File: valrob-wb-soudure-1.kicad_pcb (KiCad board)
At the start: 2 copper layers, 85 x 50 mm, 35 parts, among them J1 Conn_01x03, J2 Conn_01x06, J3 Conn_01x02, J4 Conn_01x02, J5 Conn_01x02, J6 Conn_01x02, Q1 2N7000, SW1 SW_Push, SW2 SW_Push, SW3 SW_Push, SW4 SW_Push

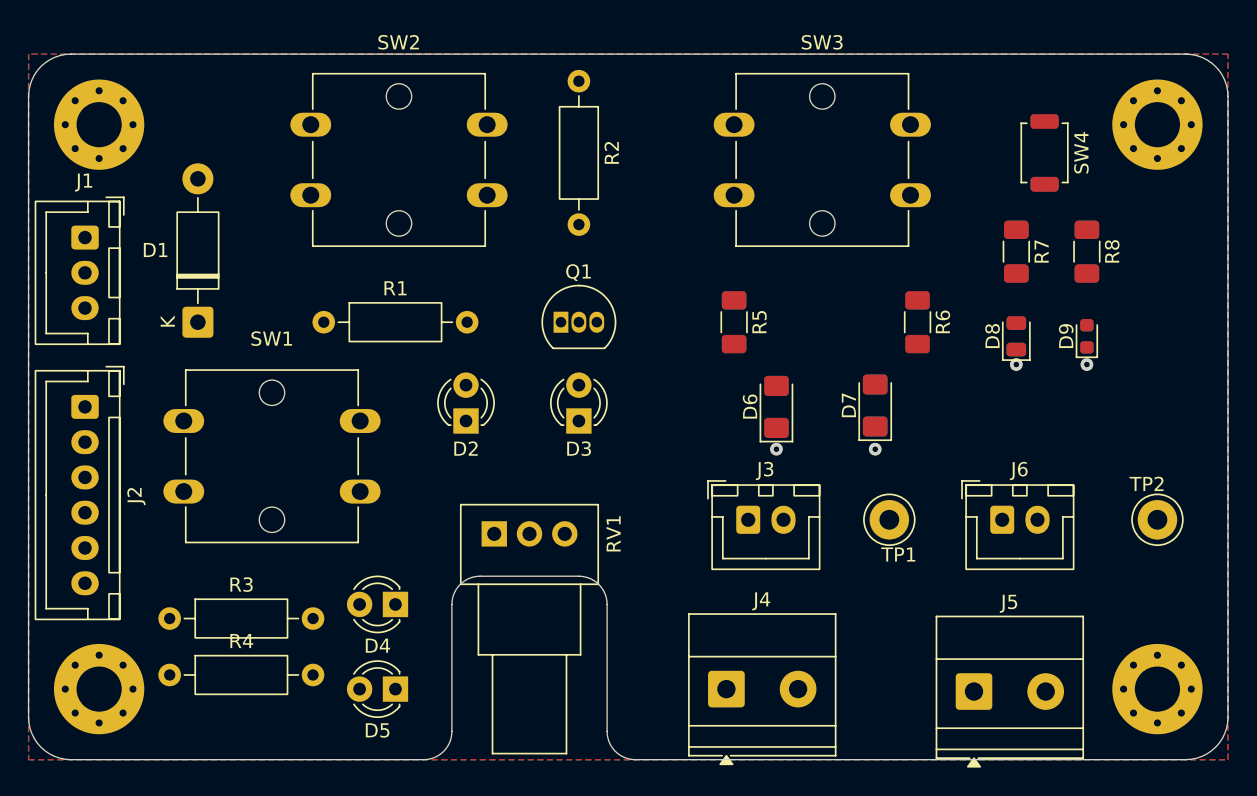
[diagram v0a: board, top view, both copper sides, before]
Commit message: pcb: add routing
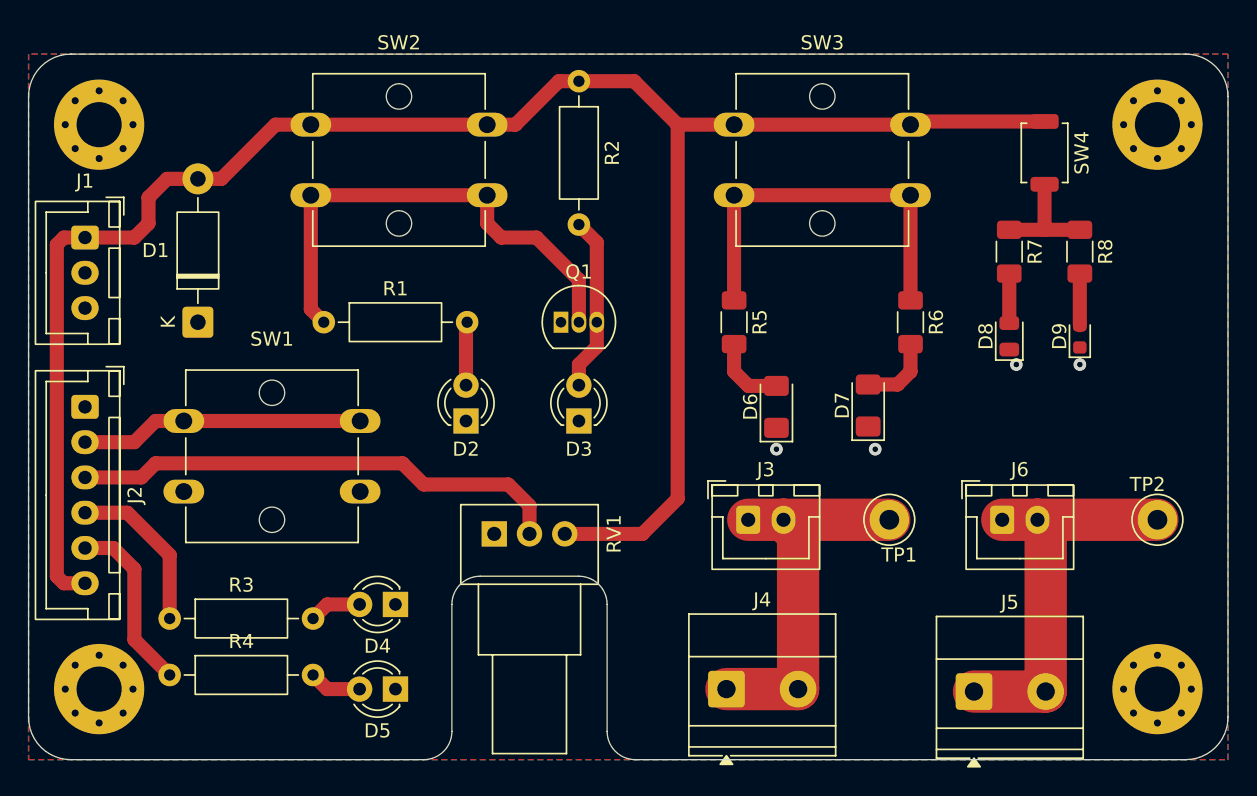
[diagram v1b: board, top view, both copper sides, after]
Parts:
- moved D7 0.50 mm to (107.5, 117.9)
- moved D8 0.50 mm to (117.5, 113.0)
- moved D9 0.50 mm to (122.5, 113.0)
- moved R6 0.50 mm to (110.5, 112.0)
- moved R7 0.50 mm to (117.5, 107.0)
- moved R8 0.50 mm to (122.5, 107.0)
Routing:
- net +5V: track 0.00 -> 138.5 mm
- net Net-(J2-Pin_3): track 0.00 -> 35.2 mm
- net Net-(Q1-G): track 0.00 -> 35.0 mm
- net Net-(J5-Pin_1): track 0.00 -> 28.5 mm
- net Net-(J3-Pin_1): track 0.00 -> 27.5 mm
- net Net-(R5-Pad1): track 0.00 -> 27.4 mm
- net Net-(J2-Pin_2): track 0.00 -> 20.1 mm
- net /RED: track 0.00 -> 12.7 mm
- net Net-(D3-A): track 0.00 -> 12.4 mm
- net /BLUE: track 0.00 -> 11.7 mm
- net Net-(R7-Pad1): track 0.00 -> 8.23 mm
- net Net-(D6-A): track 0.00 -> 5.37 mm
- net Net-(D7-A): track 0.00 -> 5.33 mm
- net Net-(D2-A): track 0.00 -> 4.49 mm
- net Net-(D5-A): track 0.00 -> 3.71 mm
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
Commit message: pcb(silk): clean reference designators
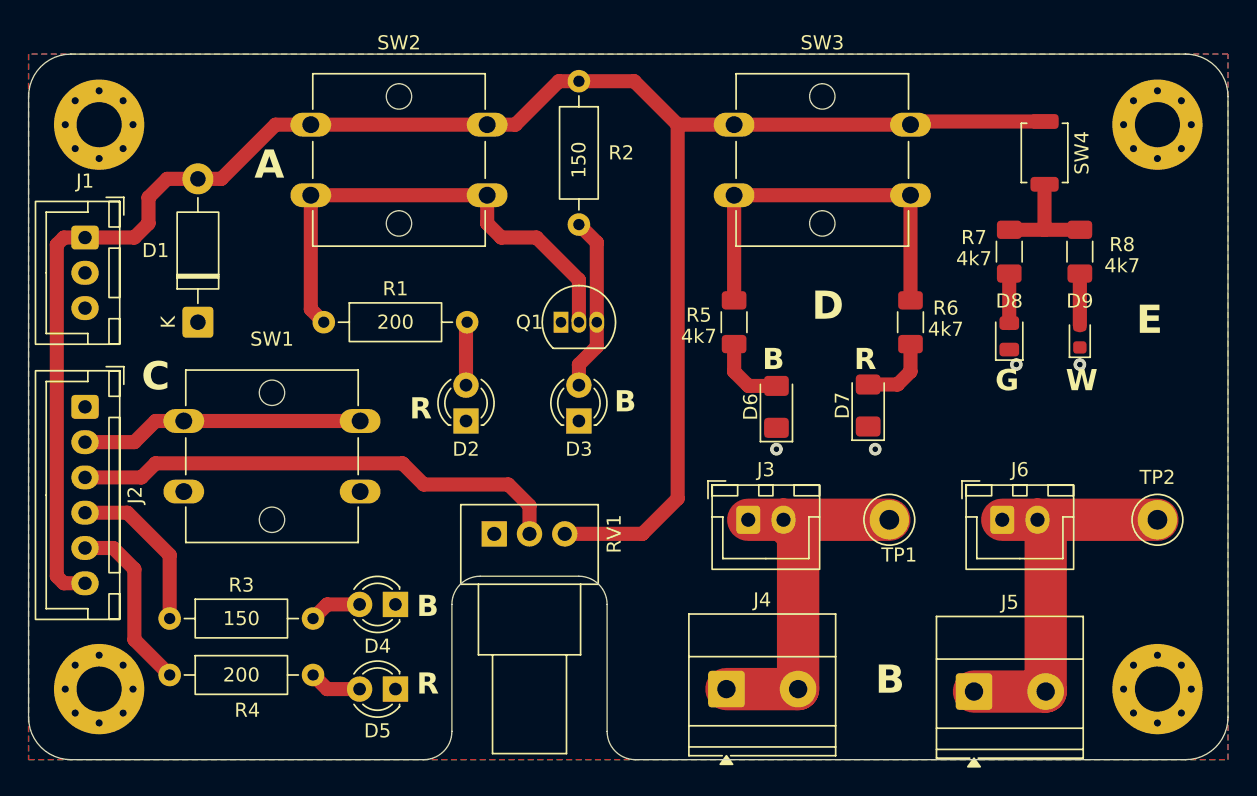
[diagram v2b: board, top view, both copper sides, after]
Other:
- board text added: "A"
- board text added: "B"
- board text added: "C"
- board text added: "D"
- board text added: "E"
- board text added: "G"
- board text added: "R"
- board text added: "W"
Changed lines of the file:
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@@
 		(tags "resistor handsolder")
 		(property "Reference" "R7"
-			(at 0 -1.83 90)
+			(at -1 2.5 180)
 			(layer "F.SilkS")
 			(effects
@@
 		)
 		(property "Value" "4k7"
-			(at 0 1.83 90)
-			(layer "F.Fab")
+			(at 0.5 2.5 180)
+			(layer "F.SilkS")
 			(effects
 				(font
@@
 		(tags "resistor handsolder")
 		(property "Reference" "R6"
-			(at 0 -1.83 90)
+			(at -1 -2.5 0)
 			(layer "F.SilkS")
 			(effects
@@
 		)
 		(property "Value" "4k7"
-			(at 0 1.83 90)
-			(layer "F.Fab")
+			(at 0.5 -2.5 0)
+			(layer "F.SilkS")
 			(effects
 				(font
@@
 		(tags "LED")
 		(property "Reference" "D8"
-			(at 0 -1.65 90)
+			(at 2.5 0 180)
 			(layer "F.SilkS")
 			(effects
@@
 		)
 		(property "Value" "200"
-			(at 5.08 2.37 0)
-			(layer "F.Fab")
+			(at 5.08 0 0)
+			(layer "F.SilkS")
 			(effects
 				(font
@@
 		(tags "LED")
 		(property "Reference" "D9"
-			(at 0 -1.43 90)
+			(at 2.5 0 180)
 			(layer "F.SilkS")
 			(effects
@@
 		(tags "test point wire loop bead")
 		(property "Reference" "TP2"
-			(at 0.7 2.5 0)
+			(at 0 3 0)
 			(layer "F.SilkS")
 			(effects
@@
 		(tags "Resistor Axial_DIN0207 series Axial Horizontal pin pitch 10.16mm 0.25W = 1/4W length 6.3mm diameter 2.5mm")
 		(property "Reference" "R4"
-			(at 5.08 -2.37 0)
+			(at 5.5 2.5 0)
 			(layer "F.SilkS")
 			(effects
@@
 		)
 		(property "Value" "200"
-			(at 5.08 2.37 0)
-			(layer "F.Fab")
+			(at 5.08 0 0)
+			(layer "F.SilkS")
 			(effects
 				(font
@@
 		(tags "to-92 sc-43 sc-43a sot54 PA33 transistor")
 		(property "Reference" "Q1"
-			(at 1.27 -3.56 0)
+			(at -2.23 0 0)
 			(layer "F.SilkS")
 			(effects
@@
 		(tags "resistor handsolder")
 		(property "Reference" "R8"
-			(at 0 -1.83 90)
+			(at -0.5 -3 180)
 			(layer "F.SilkS")
 			(effects
@@
 		)
 		(property "Value" "4k7"
-			(at 0 1.83 90)
-			(layer "F.Fab")
+			(at 1 -3 180)
+			(layer "F.SilkS")
 			(effects
 				(font
@@
 		(tags "resistor handsolder")
 		(property "Reference" "R5"
-			(at 0 -1.83 90)
+			(at -0.5 2.5 180)
 			(layer "F.SilkS")
 			(effects
@@
 		)
 		(property "Value" "4k7"
-			(at 0 1.83 90)
-			(layer "F.Fab")
+			(at 1 2.5 180)
+			(layer "F.SilkS")
 			(effects
 				(font
@@
 		(tags "Resistor Axial_DIN0207 series Axial Horizontal pin pitch 10.16mm 0.25W = 1/4W length 6.3mm diameter 2.5mm")
 		(property "Reference" "R2"
-			(at 5.08 -2.37 90)
+			(at 5.08 -3 180)
 			(layer "F.SilkS")
 			(effects
@@
 		)
 		(property "Value" "150"
-			(at 5.08 2.37 90)
-			(layer "F.Fab")
+			(at 5.58 0 90)
+			(layer "F.SilkS")
 			(effects
 				(font
@@
 		)
 		(property "Value" "150"
-			(at 5.08 2.37 0)
-			(layer "F.Fab")
+			(at 5.08 0 0)
+			(layer "F.SilkS")
 			(effects
 				(font
@@
 		(layer "Edge.Cuts")
 	)
+	(gr_text "R"
+		(at 75 119 0)
+		(layer "F.SilkS")
+		(effects
+			(font
+				(size 1.5 1.5)
+				(bold yes)
+			)
+			(justify left bottom)
+		)
+	)
+	(gr_text "B"
+		(at 75.5 133 0)
+		(layer "F.SilkS")
+		(effects
+			(font
+				(size 1.5 1.5)
+				(bold yes)
+			)
+			(justify left bottom)
+		)
+	)
+	(gr_text "R"
+		(at 75.5 138.5 0)
+		(layer "F.SilkS")
+		(effects
+			(font
+				(size 1.5 1.5)
+				(bold yes)
+			)
+			(justify left bottom)
+		)
+	)
+	(gr_text "B"
+		(at 89.5 118.5 0)
+		(layer "F.SilkS")
+		(effects
+			(font
+				(size 1.5 1.5)
+				(bold yes)
+			)
+			(justify left bottom)
+		)
+	)
+	(gr_text "B"
+		(at 100 115.5 0)
+		(layer "F.SilkS")
+		(effects
+			(font
+				(size 1.5 1.5)
+				(bold yes)
+			)
+			(justify left bottom)
+		)
+	)
+	(gr_text "R"
+		(at 106.5 115.5 0)
+		(layer "F.SilkS")
+		(effects
+			(font
+				(size 1.5 1.5)
+				(bold yes)
+			)
+			(justify left bottom)
+		)
+	)
+	(gr_text "G"
+		(at 116.5 117 0)
+		(layer "F.SilkS")
+		(effects
+			(font
+				(size 1.5 1.5)
+				(bold yes)
+			)
+			(justify left bottom)
+		)
+	)
+	(gr_text "W"
+		(at 121.5 117 0)
+		(layer "F.SilkS")
+		(effects
+			(font
+				(size 1.5 1.5)
+				(bold yes)
+			)
+			(justify left bottom)
+		)
+	)
+	(gr_text "C"
+		(at 56 117 0)
+		(layer "F.SilkS" knockout)
+		(effects
+			(font
+				(size 2 2)
+				(bold yes)
+			)
+			(justify left bottom)
+		)
+	)
+	(gr_text "A"
+		(at 64 102 0)
+		(layer "F.SilkS" knockout)
+		(effects
+			(font
+				(size 2 2)
+				(bold yes)
+			)
+			(justify left bottom)
+		)
+	)
+	(gr_text "D"
+		(at 103.5 112 0)
+		(layer "F.SilkS" knockout)
+		(effects
+			(font
+				(size 2 2)
+				(bold yes)
+			)
+			(justify left bottom)
+		)
+	)
+	(gr_text "B"
+		(at 108 138.5 0)
+		(layer "F.SilkS" knockout)
+		(effects
+			(font
+				(size 2 2)
+				(bold yes)
+			)
+			(justify left bottom)
+		)
+	)
+	(gr_text "E"
+		(at 126.5 113 0)
+		(layer "F.SilkS" knockout)
+		(effects
+			(font
+				(size 2 2)
+				(bold yes)
+			)
+			(justify left bottom)
+		)
+	)
 	(via

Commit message: pcb(silk): add user txt
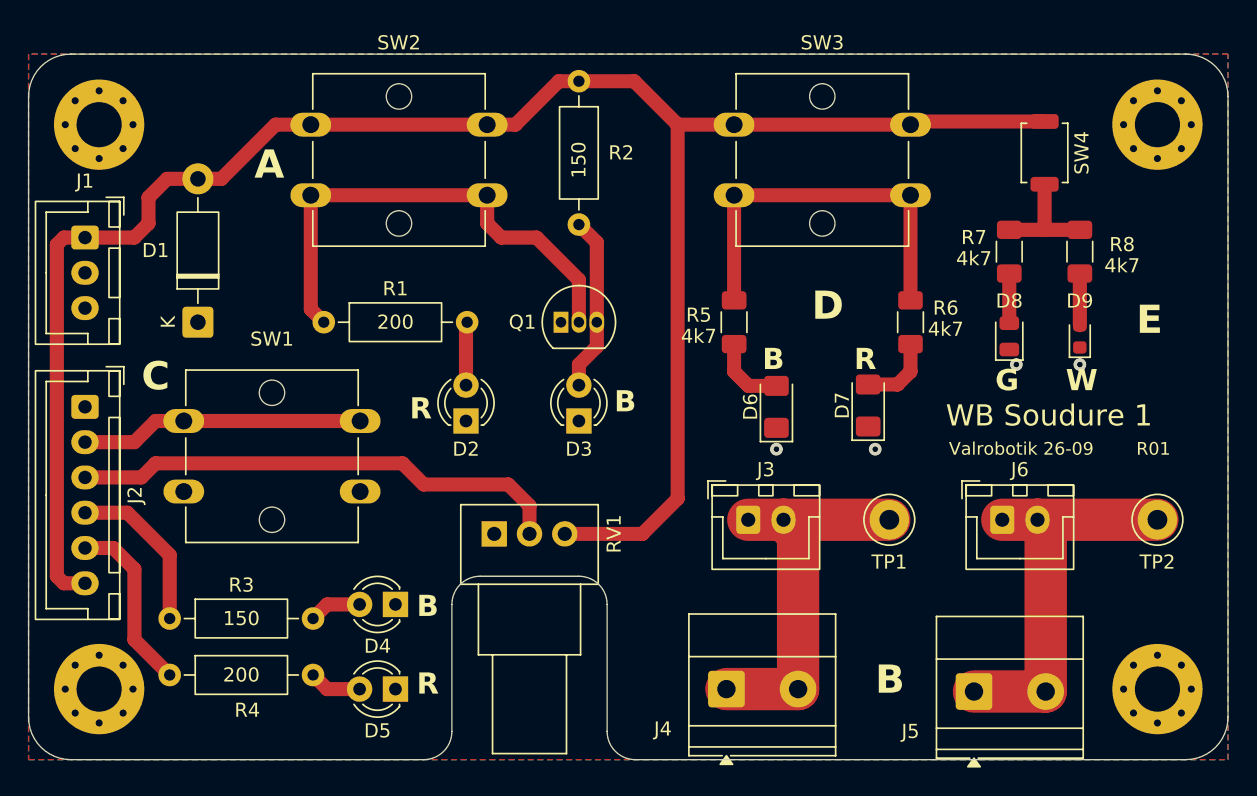
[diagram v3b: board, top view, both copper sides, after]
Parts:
- added G***: LOGO, LOGO, B.Cu at (121.5, 106.5)
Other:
- board text added: "+"
- board text added: "-"
- board text added: "1"
- board text added: "2"
- board text added: "?"
- board text added: "JLCJLCJLCJLC"
- board text added: "PWR"
- board text added: "R01"
- board text added: "Valrob WB Soudure 1"
- board text added: "Valrobotik 26-09"
- board text added: "WB Soudure 1"
